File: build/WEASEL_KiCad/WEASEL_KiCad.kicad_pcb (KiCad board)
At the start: 2 copper layers, 325 x 180 mm, 133 parts, among them J1 MIDI IN, J10 LPG_LEVEL2CTRL, J14 SEQ_OUTPUT2, J15 SEQ_OUTPUT3, J16 EG_OUTPUT1, J17 EG_OUTPUT2, J18 EG_OUTPUT3, J19 PLSR_OUTPUT1, J2 STEREO_OUTPUT, J20 PLSR_OUTPUT2, J21 PLSR_OUTPUT3, J22 RNDM_OUTPUT1, J23 RNDM_OUTPUT2, J24 RNDM_OUTPUT3, J3 SEQ_OUTPUT1, J4 PLSR_PERIODCTRL, J5 MODOSC_FREQCTRL, J6 MODOSC_MODCTRL, J7 COMPOSC_PITCHCTRL, J8 COMPOSC_WAVEFOLDERCTRL, J9 LPG_LEVEL1CTRL, SW1 SQ_TOGGLESTEP1, SW2 SEQ_TRIGGERSELECT, SW3 SQ_TOGGLESTEP2, SW31 EG_TRIGGERSELECT, SW32 EG_MODESELECT, SW33 PLSR_TRIGGERSELECT, SW34 PLSR_MODE, SW35 MODOSC_MIDITOGGLE, SW36 MODOSC_PITCHTRANGE, SW37 COMPLEXOSC_MIDITOGGLE, SW38 COMPLEXOSC_POLARITY, SW39 COMPLEXOSC_WAVETOGGLE, SW4 SQ_TOGGLESTEP3, SW40 LPG_GATE1MODE, SW41 LPG_GATE2MODE, SW42 RNDMVOLTAGE_TRIGGERSELECT, SW43 CLOCK_SYNCTOGGLE, SW5 SQ_TOGGLESTEP4, SW6 SEQ_STAGES, SW7 SQ_TOGGLESTEP5, U3 6N138

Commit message: Schematic and PCB Update
- PCB changes
-
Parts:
- added C27: 10nF, DIYSynthMNL:C_Rect_L7.0mm_W2.0mm_P5.00mm_BigPads, F.Cu at (332.3, 173.6)
- added RV27: REVERB_MIX, DIYSynthMNL:Potentiometer_RV09_BigPads, F.Cu at (338.0, 120.0)
- added U1: CD74HC4067, CD74HC4067 MUX:CD74HC4067, F.Cu at (280.9, 183.0)
- added U2: CD74HC4067, CD74HC4067 MUX:CD74HC4067, F.Cu at (325.9, 183.1)
- moved D5 599.2 mm to (337.0, 28.8)
- moved D8 595.6 mm to (333.0, 36.8)
- moved D7 594.9 mm to (333.0, 39.2)
- moved D6 594.4 mm to (333.0, 41.8)
- moved D4 593.6 mm to (333.0, 44.2)
- moved D3 593.1 mm to (332.9, 46.8)
- moved D2 592.8 mm to (332.9, 49.2)
- moved D1 592.4 mm to (332.9, 51.8)
- moved C26 572.0 mm to (329.8, 173.6), turned to 90 degrees
- moved C25 569.3 mm to (327.1, 173.6), turned to 90 degrees
- moved C24 566.9 mm to (324.6, 173.6), turned to 90 degrees
- moved C23 564.5 mm to (322.1, 173.6), turned to 90 degrees
- moved C22 562.2 mm to (319.6, 173.6), turned to 90 degrees
- moved C18 559.9 mm to (309.3, 173.6), turned to 90 degrees
- moved C21 559.8 mm to (317.1, 173.6), turned to 90 degrees
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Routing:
- net B3: track 0.00 -> 37.2 mm
- net B0: track 0.00 -> 37.2 mm
- net B2: track 0.00 -> 37.2 mm
- net B1: track 0.00 -> 37.2 mm
- net Net-(D8-A): track 0.00 -> 11.4 mm
- net Net-(D7-A): track 0.00 -> 11.4 mm
- net Net-(D6-A): track 0.00 -> 11.4 mm
- net Net-(D4-A): track 0.00 -> 11.4 mm
- net Net-(D3-A): track 0.00 -> 11.4 mm
- net Net-(D2-A): track 0.00 -> 11.4 mm
- net Net-(D1-A): track 0.00 -> 11.4 mm
- net A6: track 0.00 -> 3.54 mm
- net A5: track 0.00 -> 3.53 mm
- net A3: track 0.00 -> 3.52 mm
- net A4: track 0.00 -> 3.51 mm
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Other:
- board size 325 x 180 mm -> 329.8 x 180 mm

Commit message: PCB Layout v1.0
- Finished PCB Layout v1.0
- Gerbers generated
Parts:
- moved D5 285.3 mm to (52.0, 42.4), turned to -90 degrees
- moved D43 237.0 mm to (312.5, 102.4), turned to -90 degrees
- moved D45 229.9 mm to (52.6, 59.0), turned to 180 degrees
- moved D46 225.3 mm to (72.6, 59.0), turned to 180 degrees
- moved D47 222.5 mm to (92.6, 59.0), turned to 180 degrees
- moved D49 222.4 mm to (133.1, 59.0), turned to 180 degrees
- moved D48 221.6 mm to (112.6, 59.0), turned to 180 degrees
- moved D41 209.6 mm to (282.5, 102.4), turned to -90 degrees
- moved D42 205.9 mm to (132.5, 42.4), turned to -90 degrees
- moved D39 194.2 mm to (212.5, 62.4), turned to -90 degrees
- moved D40 192.8 mm to (262.5, 102.4), turned to -90 degrees
- moved D38 177.2 mm to (172.5, 62.4), turned to -90 degrees
- moved D37 160.1 mm to (232.5, 102.4), turned to -90 degrees
- moved D31 159.1 mm to (52.0, 102.2), turned to -90 degrees
- moved D35 153.5 mm to (212.5, 102.5), turned to -90 degrees
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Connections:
- U1 pad C0: Net-(U1-i0) -> (no net)
- U1 pad C1: Net-(U1-i1) -> (no net)
- U1 pad C10: Net-(U1-i10) -> (no net)
- U1 pad C11: Net-(U1-i11) -> (no net)
- U1 pad C12: Net-(U1-i12) -> (no net)
- U1 pad C13: Net-(U1-i13) -> (no net)
- U1 pad C14: Net-(U1-i14) -> (no net)
- U1 pad C15: Net-(U1-i15) -> (no net)
- U1 pad C2: Net-(U1-i2) -> (no net)
- U1 pad C3: Net-(U1-i3) -> (no net)
- U1 pad C4: Net-(U1-i4) -> (no net)
- U1 pad C5: Net-(U1-i5) -> (no net)
- U1 pad C6: Net-(U1-i6) -> (no net)
- U1 pad C7: Net-(U1-i7) -> (no net)
- U1 pad C8: Net-(U1-i8) -> (no net)
- U1 pad C9: Net-(U1-i9) -> (no net)
- U1 pad EN: GND -> (no net)
- U1 pad GND: GND -> (no net)
- U1 pad S0: MUX1_S0 -> (no net)
- U1 pad S1: MUX1_S2 -> (no net)
- U1 pad S2: MUX1_S2 -> (no net)
- U1 pad S3: MUX1_S3 -> (no net)
- U1 pad SIG: MUX1_SIGNAL -> (no net)
- U1 pad VCC: Vcc -> (no net)
- U2 pad C0: Net-(U2-i0) -> (no net)
- U2 pad C1: Net-(U2-i1) -> (no net)
- U2 pad C10: Net-(U2-i10) -> (no net)
- U2 pad C2: Net-(U2-i2) -> (no net)
- U2 pad C3: Net-(U2-i3) -> (no net)
- U2 pad C4: Net-(U2-i4) -> (no net)
- U2 pad C5: Net-(U2-i5) -> (no net)
- U2 pad C6: Net-(U2-i6) -> (no net)
- U2 pad C7: Net-(U2-i7) -> (no net)
- U2 pad C8: Net-(U2-i8) -> (no net)
- U2 pad C9: Net-(U2-i9) -> (no net)
- U2 pad EN: GND -> (no net)
- U2 pad GND: GND -> (no net)
- U2 pad S0: MUX2_S0 -> (no net)
- U2 pad S1: MUX2_S1 -> (no net)
- U2 pad S2: MUX2_S2 -> (no net)
- U2 pad S3: MUX2_S3 -> (no net)
- U2 pad SIG: MUX2_SIGNAL -> (no net)
- U2 pad VCC: Vcc -> (no net)
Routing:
- net Vcc: track 3.46 -> 1390.5 mm, vias 0 -> 16
- net MUX1_S1: track 0.00 -> 712.3 mm, vias 0 -> 1
- net MUX1_S0: track 0.00 -> 707.1 mm, vias 0 -> 1
- net Net-(D8-A): track 11.4 -> 688.7 mm, vias 0 -> 1
- net X0: track 3.45 -> 671.8 mm
- net Net-(D7-A): track 11.4 -> 671.3 mm, vias 0 -> 1
- net X2: track 3.06 -> 643.8 mm
- net Net-(U1-i4): track 3.04 -> 462.3 mm
- net B2: track 37.2 -> 480.7 mm
- net Net-(U1-i3): track 2.75 -> 434.6 mm
- net X1: track 3.45 -> 424.5 mm
- net X3: track 3.05 -> 422.3 mm, vias 0 -> 4
- net Net-(U1-i2): track 3.03 -> 407.9 mm
- net B0: track 37.2 -> 440.2 mm
- net B3: track 37.2 -> 440.0 mm, vias 0 -> 2
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- added copper zone on B.Cu, net GND
- added copper zone on F.Cu, net GND
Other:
- board size 329.8 x 180 mm -> 342.8 x 184 mm

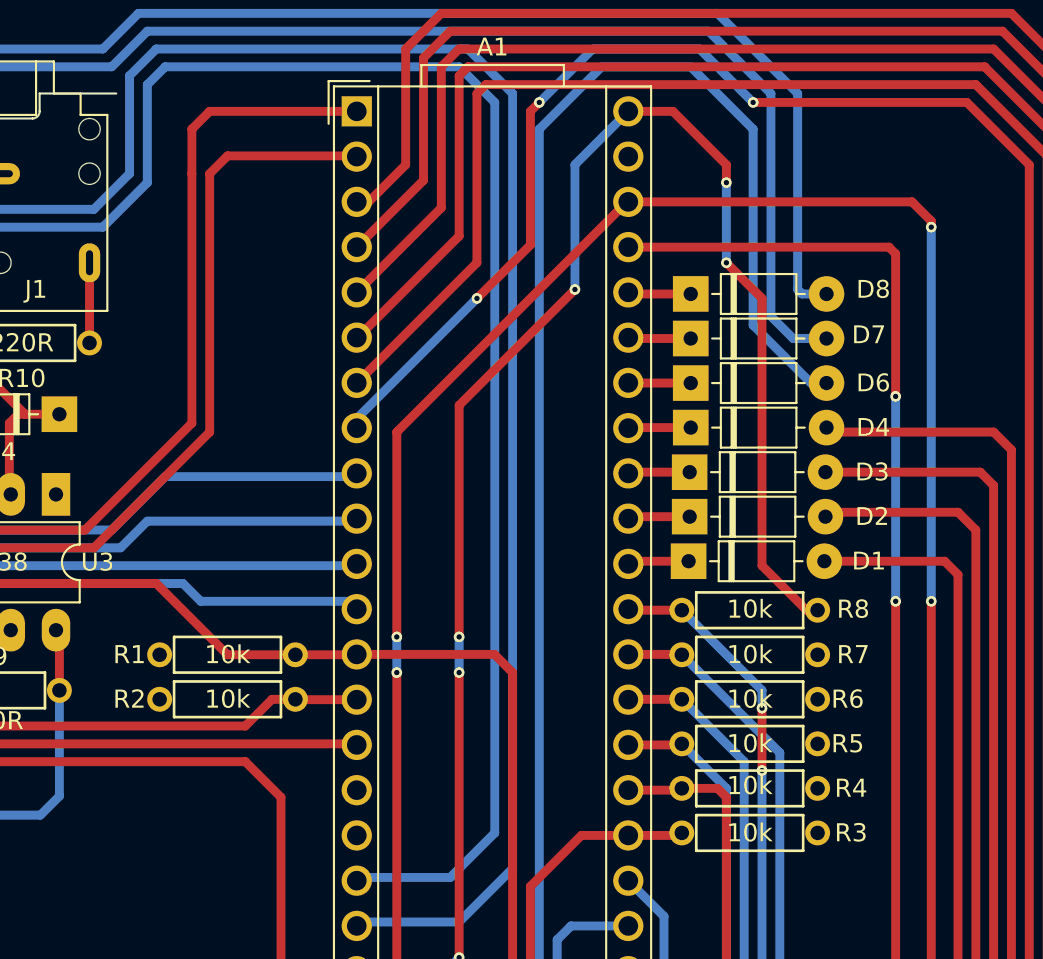
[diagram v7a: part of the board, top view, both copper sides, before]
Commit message: PCB & Schematic updates
Created prototype virtual modular matrix
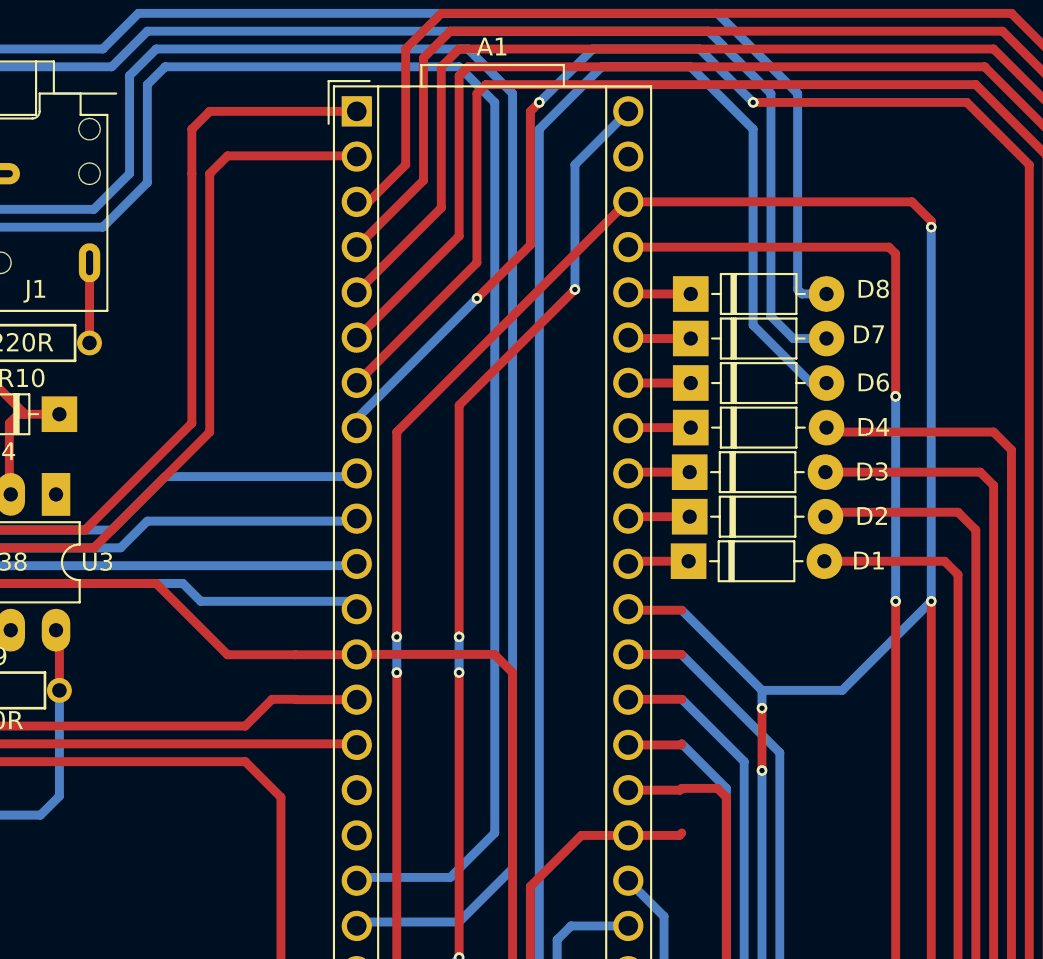
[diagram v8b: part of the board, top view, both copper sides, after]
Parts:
- removed R1, R2, R3, R4, R5, R6, R7, R8: 10k, PCM_4ms_Resistor:R_Axial_DIN0207_L6.3mm_D2.5mm_P7.62mm_Horizontal
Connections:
- A1 pad 13: X0 -> B0
- A1 pad 14: X1 -> B0
- A1 pad 24: X2 -> B0
- A1 pad 25: X3 -> B0
- A1 pad 27: B1 -> B0
- A1 pad 28: B2 -> B0
- A1 pad 29: B3 -> B0
- A1 pad 38: Vcc -> B0
- J16 pad S: B1 -> B0
- J16 pad T: B1 -> B0
- J16 pad TN: B1 -> B0
- J17 pad S: B1 -> B0
- J17 pad T: B1 -> B0
- J17 pad TN: B1 -> B0
- J18 pad S: B1 -> B0
- J18 pad T: B1 -> B0
- J18 pad TN: B1 -> B0
- J19 pad S: B2 -> B0
- J19 pad T: B2 -> B0
- J19 pad TN: B2 -> B0
- J20 pad S: B2 -> B0
- J20 pad T: B2 -> B0
- J20 pad TN: B2 -> B0
- J21 pad S: B2 -> B0
- J21 pad T: B2 -> B0
- J21 pad TN: B2 -> B0
- J22 pad S: B3 -> B0
- J22 pad T: B3 -> B0
- J22 pad TN: B3 -> B0
- J23 pad S: B3 -> B0
- J23 pad T: B3 -> B0
- J23 pad TN: B3 -> B0
- J24 pad S: B3 -> B0
- J24 pad T: B3 -> B0
- J24 pad TN: B3 -> B0
- R9 pad 1: Vcc -> B0
- RV1 pad 3: Vcc -> B0
- RV10 pad 3: Vcc -> B0
- RV11 pad 3: Vcc -> B0
- RV12 pad 1: GND -> B0
- RV12 pad 3: Vcc -> GND
- RV13 pad 3: Vcc -> B0
- RV14 pad 3: Vcc -> B0
- RV15 pad 3: Vcc -> B0
- RV16 pad 3: Vcc -> B0
- RV17 pad 3: Vcc -> B0
- RV18 pad 3: Vcc -> B0
- RV19 pad 3: Vcc -> B0
- RV2 pad 3: Vcc -> B0
- RV20 pad 3: Vcc -> B0
- RV21 pad 3: Vcc -> B0
- RV22 pad 3: Vcc -> B0
- RV23 pad 3: Vcc -> B0
- RV24 pad 3: Vcc -> B0
- RV25 pad 3: Vcc -> B0
- RV26 pad 3: Vcc -> B0
- RV27 pad 3: Vcc -> B0
- RV3 pad 3: Vcc -> B0
- RV4 pad 3: Vcc -> B0
- RV5 pad 3: Vcc -> B0
- RV6 pad 3: Vcc -> B0
- RV7 pad 3: Vcc -> B0
- RV8 pad 3: Vcc -> B0
- RV9 pad 3: Vcc -> B0
- SW1 pad 2: X3 -> B0
- SW2 pad 1: X0 -> B0
- SW3 pad 2: X0 -> B0
- SW31 pad 1: X2 -> B0
- SW32 pad 1: X3 -> B0
- SW33 pad 1: X0 -> B0
- SW34 pad 1: X1 -> B0
- SW35 pad 1: X2 -> B0
- SW36 pad 1: X3 -> B0
- SW37 pad 1: X0 -> B0
- SW38 pad 1: X1 -> B0
- SW39 pad 1: X2 -> B0
- SW4 pad 2: X1 -> B0
- SW40 pad 1: X3 -> B0
- SW41 pad 1: X0 -> B0
- SW42 pad 1: X1 -> B0
- SW43 pad 1: X2 -> B0
- SW5 pad 2: X2 -> B0
- SW6 pad 1: X1 -> B0
- SW7 pad 2: X3 -> B0
- U3 pad 8: Vcc -> B0
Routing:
- net B0: track 440.2 -> 3942.3 mm, vias 0 -> 22
- net Vcc: track 1390.5 -> 0.00 mm, vias 16 -> 0
- net (no net): track 0.00 -> 1390.5 mm
- net X0: track 671.8 -> 0.00 mm
- net X2: track 643.8 -> 0.00 mm
- net B2: track 480.7 -> 0.00 mm
- net B3: track 440.0 -> 0.00 mm, vias 2 -> 0
- net X1: track 424.5 -> 0.00 mm
- net X3: track 422.3 -> 0.00 mm, vias 4 -> 0
- net B1: track 407.4 -> 0.00 mm
- net GND: track 133.2 -> 99.0 mm, vias 9 -> 7
